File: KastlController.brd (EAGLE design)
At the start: 100 x 80 mm, 17 parts

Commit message: Update KastlController.brd
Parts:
- removed GESTUREBOARD: GESTUREBOARD_INTERFACE, gestureBoardInterface_Kastl:CONNECTOR_JUMPER
- removed GESTUREBOARD_PWR: GESTUREBOARD_POWER, gestureBoardInterface_Kastl:POWER_CONNECTOR
- removed GND_PSU, VCC12: (no value), wirepad:2,54/1,0
- removed PW_REG_3_3V: STEPDOWN_5V-3_3V, 5V3_3V_stepdown:3P_PWR_REG
- added 12V_PSU: PWR_CONNECTOR, PowerConnector:2PIN_CONN
- added 5V_3V3_CONV: STEPDOWN_5V-3_3V, 5V3_3V_stepdown:3P_PWR_REG
- added C5: (no value), htl3r-discrete:C2.5-2
- added GESTURE_POWER: GESTUREBOARD_POWER, gestureBoardInterface_Kastl:POWER_CONNECTOR
- added LED1: (no value), htl3r-discrete:LED5MM
- added R1: 100k, htl3r-discrete:R-2,5
- added R2: 220k, htl3r-discrete:R-2,5
- added R3: 10k, htl3r-discrete:R-2,5
- added R4: 2k2, htl3r-discrete:R-2,5
- added REAL_TIME_CLOCK: DS3231_RTC_MODULE, DS3231_RTC:6P_HEADER
- added Y1: 32.768kHz, SparkFun-FreqCtrl:CRYSTAL-SMD-3.2X1.5MM
- LEDSTRIP_DRW, LEDSTRIP_MID, LEDSTRIP_TOP: value WS2812_JMP -> (none)
- U$1: value 3_3/5V_LEVELCONVERTER -> GESTUREBOARD; device LogicLevelConv_Kastl:12P/15.24MM -> gestureBoardInterface_Kastl:INTERFACE_AND_POWER_CONN
- moved C1 133.9 mm to (-35.6, -81.3)
- moved U$1 128.5 mm to (-132.1, -121.9)
- moved LEDSTRIP_DRW 106.7 mm to (-88.9, -127.0)
- moved LEDSTRIP_MID 106.7 mm to (-83.8, -127.0)
- moved LEDSTRIP_TOP 106.7 mm to (-78.7, -127.0)
- moved C2 48.8 mm to (-35.6, -86.4)
- moved C3 39.7 mm to (-50.8, -101.6)
- moved C4 36.6 mm to (-50.8, -106.7)
- renumbered J_BT_BOARD_1 to HC-06_BLUETOOTH
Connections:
- removed net VCC12: LEDSTRIP_DRW.VCC12, LEDSTRIP_MID.VCC12, LEDSTRIP_TOP.VCC12, VCC12.1
- removed net VCC5: ATMEGA328P.7, C1.1, C2.1, C3.1, C4.1, HC-06_BLUETOOTH.VCC, MOBILE_OUT.VBUS, PW_REG_3_3V.VIN, PW_REG_5V.VBUS, U$1.VCC5
- new net +12V: 12V_PSU.V+, LEDSTRIP_DRW.VCC12, LEDSTRIP_MID.VCC12, LEDSTRIP_TOP.VCC12
- new net +3V3: 5V_3V3_CONV.VOUT, C1.1, C2.1, GESTURE_POWER.VCC3_3, HC-06_BLUETOOTH.VCC, U$1.VCC_3V3
- new net +5V: 5V_3V3_CONV.VIN, ATMEGA328P.20, ATMEGA328P.21, ATMEGA328P.7, C3.1, C4.1, C5.1, MOBILE_OUT.VBUS, PW_REG_5V.VBUS, R3.2, REAL_TIME_CLOCK.VCC
- new net N$13: ATMEGA328P.27, REAL_TIME_CLOCK.SDA
- new net N$15: ATMEGA328P.28, REAL_TIME_CLOCK.SCL
- new net N$16: HC-06_BLUETOOTH.RX, R1.1, R2.2
- net GND: now also 12V_PSU.GND, 5V_3V3_CONV.GND, ATMEGA328P.8, C5.2, GESTURE_POWER.GND, LED1.K, R2.1, REAL_TIME_CLOCK.GND, U$1.GND, Y1.P$2; no longer GESTUREBOARD_PWR.GND, GND_PSU.1, PW_REG_3_3V.GND, U$1.GND_1, U$1.GND_2
- net N$10: now also LED1.A, R4.1; no longer ATMEGA328P.3, U$1.RXI_CH1_H
- net N$11: now also REAL_TIME_CLOCK.OSC, Y1.P$1; no longer HC-06_BLUETOOTH.TX, U$1.TXI_CH1_L
- net N$12: now also ATMEGA328P.1, R3.1; no longer HC-06_BLUETOOTH.RX, U$1.RXO_CH1_L
- net N$14: now also ATMEGA328P.2, HC-06_BLUETOOTH.TX; no longer GESTUREBOARD_PWR.VCC3_3, PW_REG_3_3V.VOUT, U$1.VCC3_3
- net N$3: now also U$1.GPIN1; no longer GESTUREBOARD.GPIN1
- net N$4: now also U$1.GPIN2; no longer GESTUREBOARD.GPIN2
- net N$5: now also U$1.GPIN3; no longer GESTUREBOARD.GPIN3
- net N$6: now also U$1.GPIN6; no longer GESTUREBOARD.GPIN6
- net N$7: now also U$1.GPIN7; no longer GESTUREBOARD.GPIN7
- net N$9: now also ATMEGA328P.3, R1.2; no longer ATMEGA328P.2, U$1.TXO_CH1_H

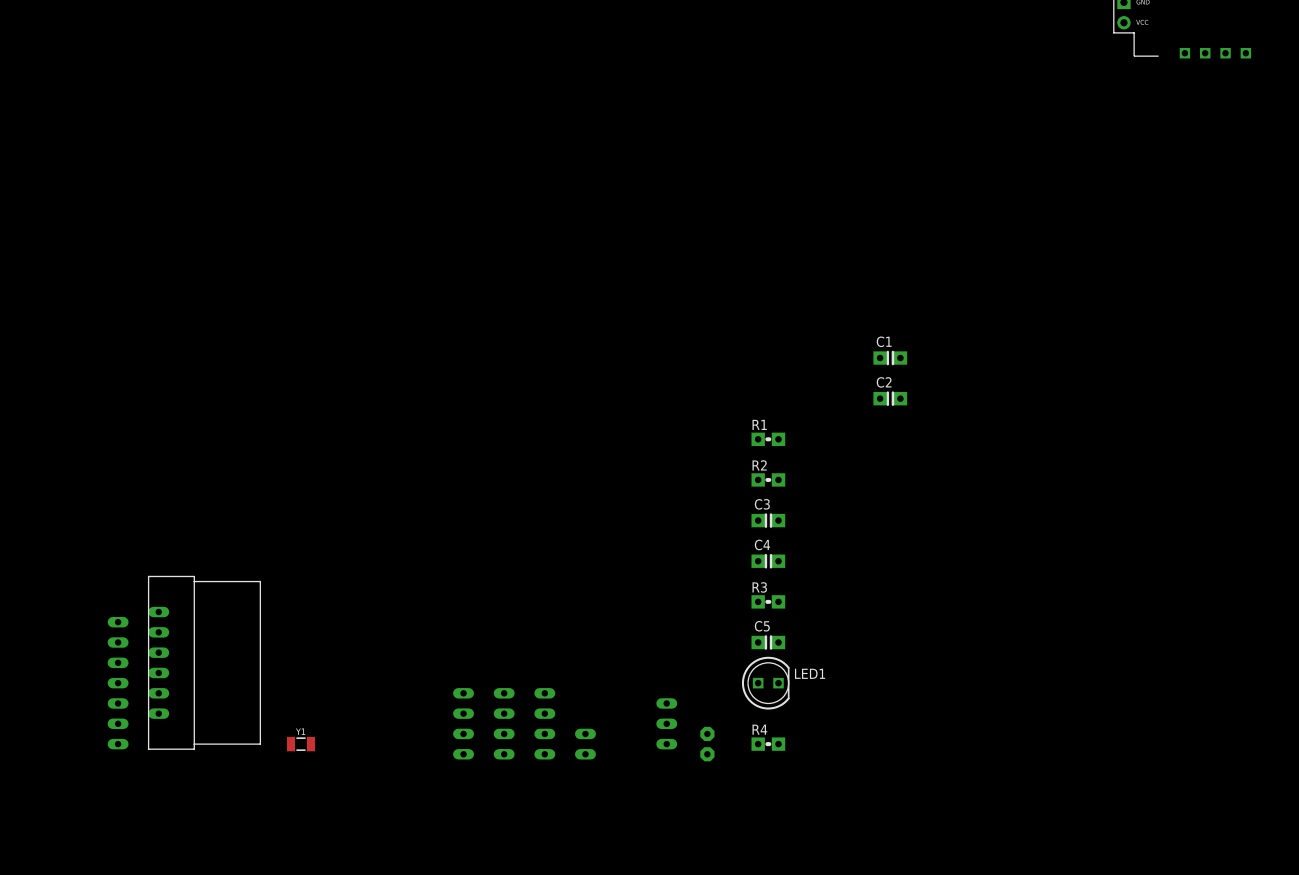
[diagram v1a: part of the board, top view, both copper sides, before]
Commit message: changed voltage regulators, cleanup
added voltage regulator libraries and changed some minor things
corrected a mistake with the oscillator of the real time clock module
(no oscillator is needed since it is already integrated)
updated readme
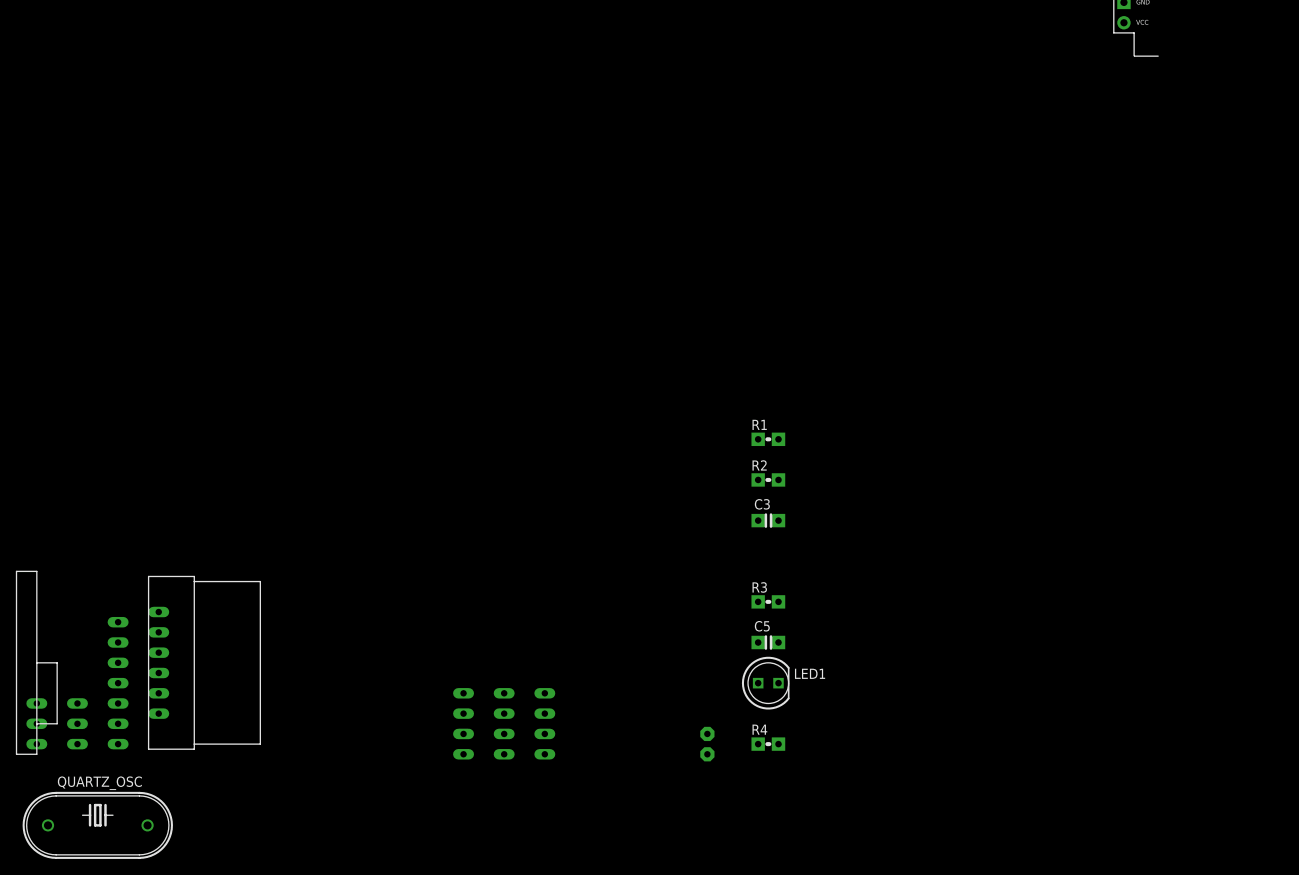
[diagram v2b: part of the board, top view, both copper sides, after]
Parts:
- removed 5V_3V3_CONV: STEPDOWN_5V-3_3V, 5V3_3V_stepdown:3P_PWR_REG
- removed C1, C2, C4: (no value), htl3r-discrete:C2.5-2
- removed GESTURE_POWER: GESTUREBOARD_POWER, gestureBoardInterface_Kastl:POWER_CONNECTOR
- removed PW_REG_5V: USB_JUMPER, SparkFun-Connectors:USB_JUMPER
- removed Y1: 32.768kHz, SparkFun-FreqCtrl:CRYSTAL-SMD-3.2X1.5MM
- added 12V->5V: VOLTAGE_REG_12V_5V, Voltage_Regulators:3_PIN_HEADER_BIG
- added 5V->3V3: VOLTAGE_REG_5V_3V3, Voltage_Regulators:3_PIN_HEADER
- added QUARTZ_OSC: 16MHz, crystal:HC33U-V
- renumbered U$1 to GESTURE_BOARD
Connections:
- removed net N$11: REAL_TIME_CLOCK.OSC, Y1.P$1
- net +12V: now also 12V->5V.PIN3
- net +3V3: now also 5V->3V3.PIN2, R4.2; no longer 5V_3V3_CONV.VOUT, C1.1, C2.1, GESTURE_POWER.VCC3_3
- net +5V: now also 12V->5V.PIN1, 5V->3V3.PIN1; no longer 5V_3V3_CONV.VIN, C4.1, PW_REG_5V.VBUS
- net GND: now also 12V->5V.PIN2, 5V->3V3.PIN3; no longer 5V_3V3_CONV.GND, C1.2, C2.2, C4.2, GESTURE_POWER.GND, PW_REG_5V.GND, Y1.P$2
